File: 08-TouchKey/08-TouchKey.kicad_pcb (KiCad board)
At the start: 2 copper layers, 90 x 60 mm, 22 parts, among them J1 AudioJack3, P1 TouchPaddles, P2 TouchPaddles, P3 TouchPaddles, P4 TouchPaddles, P5 TouchPaddles, P6 TouchPaddles, Q1 Q_Dual_PMOS_S1G1D2S2G2D1, U1 AT42QT1011-TSHR, U2 AT42QT1011-TSHR

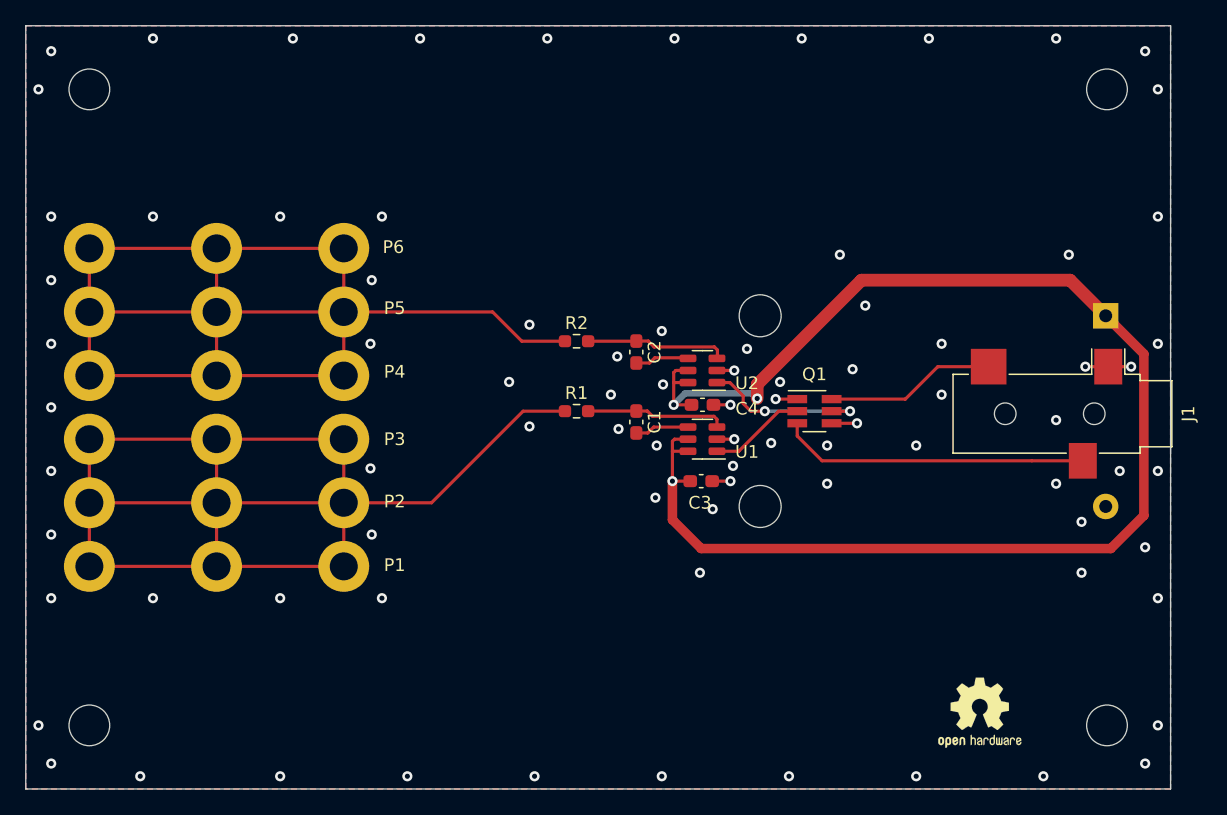
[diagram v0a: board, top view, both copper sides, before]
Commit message: Update key and paddle to add more solder pads to improve mounting
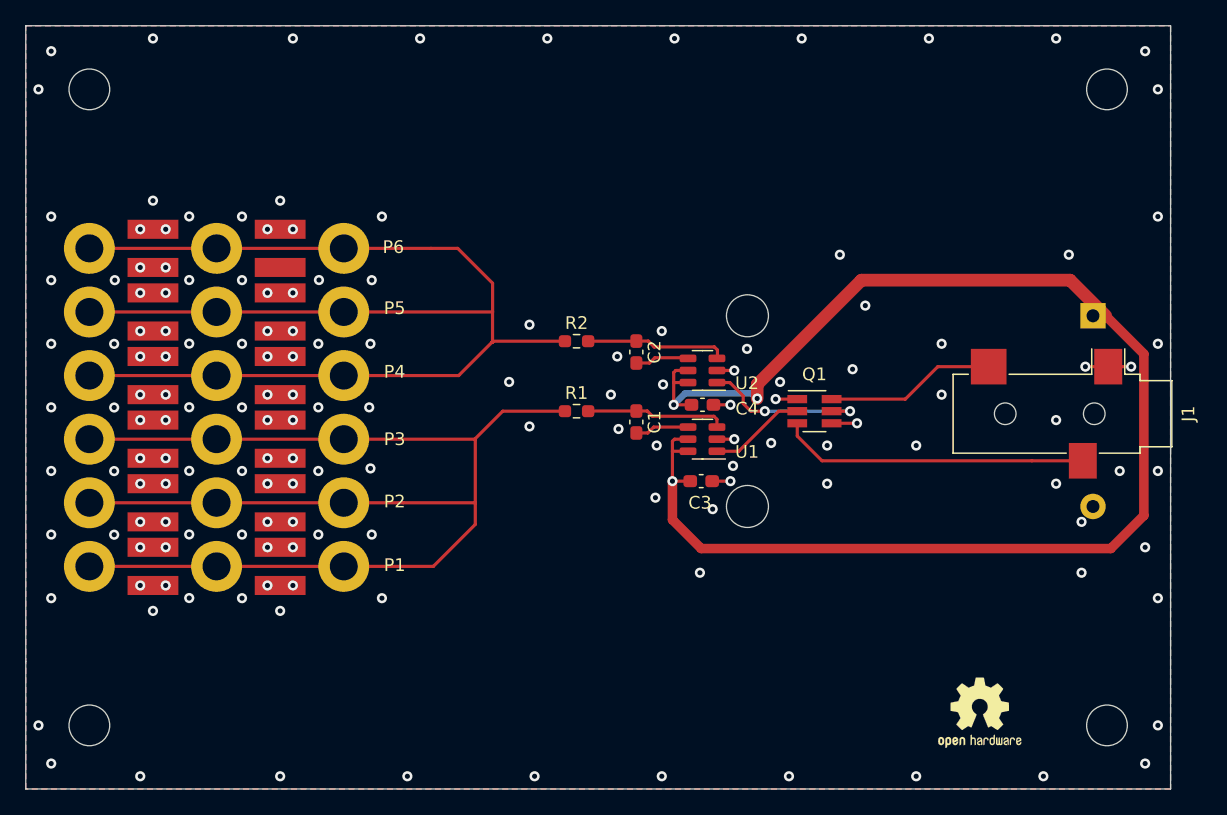
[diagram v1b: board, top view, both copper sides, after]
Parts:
- moved BT1 1.00 mm to (193.9, 97.8)
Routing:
- net Net-(R1-Pad1): track 110.4 -> 107.1 mm
- net Net-(R2-Pad1): track 108.7 -> 108.1 mm
- net GND: vias 84 -> 155
